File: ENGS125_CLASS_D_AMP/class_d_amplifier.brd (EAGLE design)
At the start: 89.8 x 64.8 mm, 24 parts, among them J1 BANANA_JACK_CT3151, J2 BANANA_JACK_CT3151, J3 BANANA_JACK_CT3151, J4 BANANA_JACK_CT3151, J5 BANANA_JACK_CT3151, J6 BANANA_JACK_CT3151, M1 BSC050NE2LSATMA1, M2 BSC050NE2LSATMA1, U1 LTC6992TSOT-23, U2 LTC4449

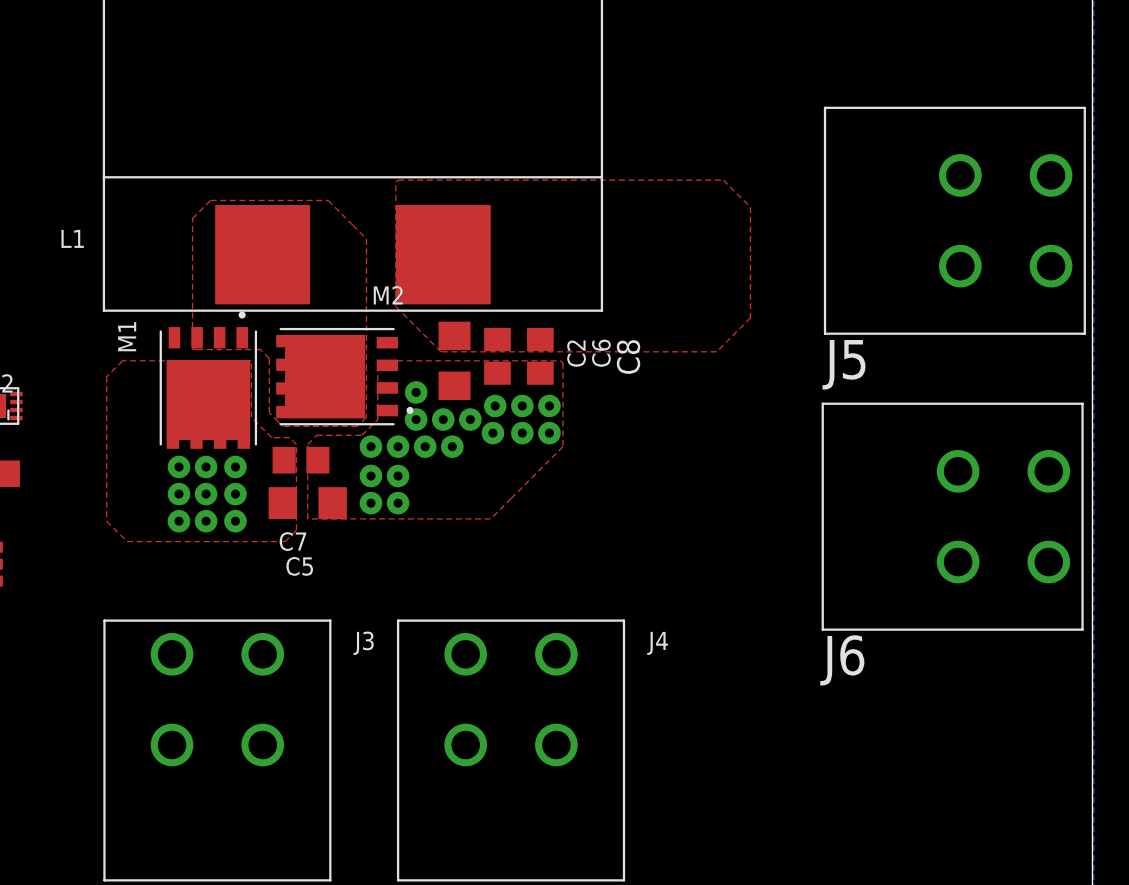
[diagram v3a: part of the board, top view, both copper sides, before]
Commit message: Routed power polygons to connectors
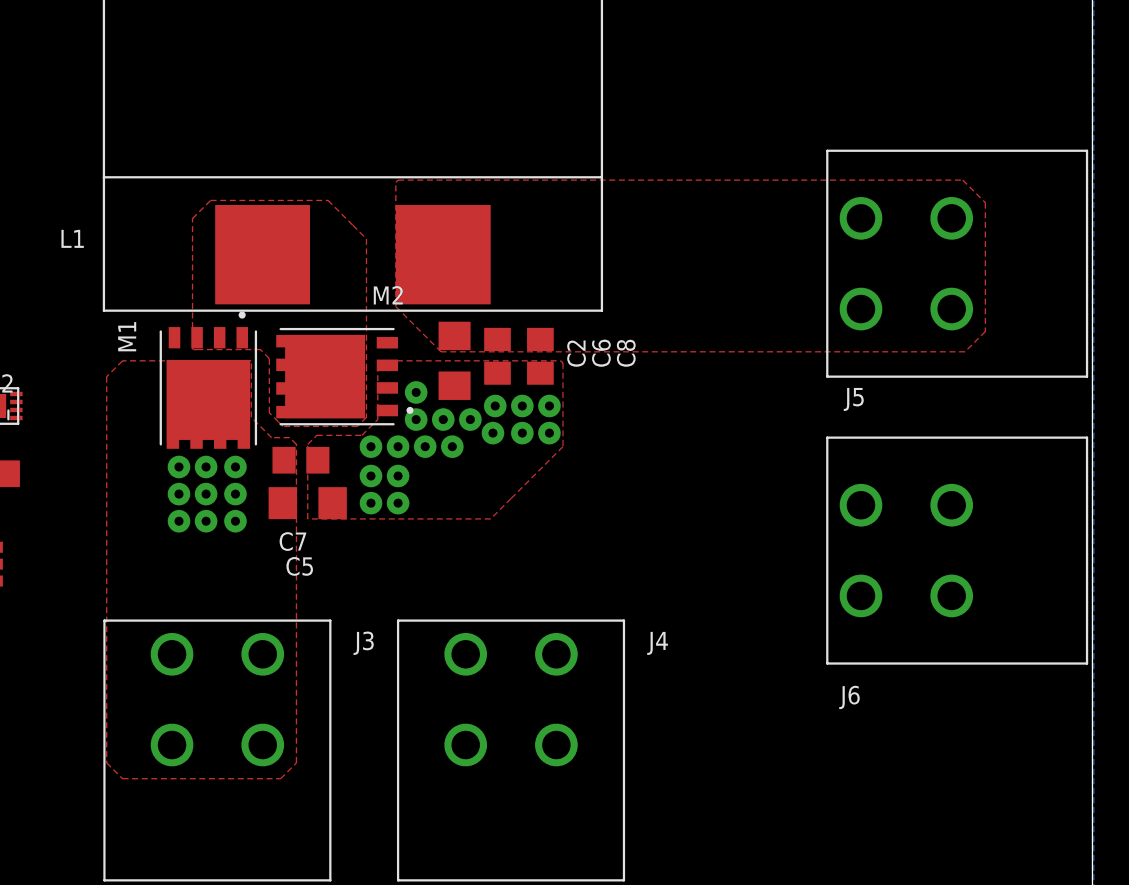
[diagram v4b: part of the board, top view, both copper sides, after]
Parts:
- moved J5 6.09 mm to (79.4, 35.9), turned to 180 degrees
- moved J6 5.78 mm to (79.4, 19.8), turned to 180 degrees
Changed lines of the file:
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@@
 <layer number="17" name="Pads" color="2" fill="1" visible="yes" active="yes"/>
 <layer number="18" name="Vias" color="2" fill="1" visible="yes" active="yes"/>
-<layer number="19" name="Unrouted" color="6" fill="1" visible="no" active="yes"/>
+<layer number="19" name="Unrouted" color="6" fill="1" visible="yes" active="yes"/>
 <layer number="20" name="Dimension" color="24" fill="1" visible="yes" active="yes"/>
 <layer number="21" name="tPlace" color="7" fill="1" visible="yes" active="yes"/>
@@
 <attribute name="NAME" x="51.18835" y="34.66365" size="1.016" layer="25" font="fixed" rot="R180"/>
 </element>
-<element name="J5" library="Engs125_lib_UPDATEFeb22" package="CT3151SP2_PCB_MOUNT" value="BANANA_JACK_CT3151" x="84.963" y="38.354" smashed="yes">
-<attribute name="NAME" x="74.803" y="29.464" size="2.1844" layer="25" font="vector"/>
-</element>
-<element name="J6" library="Engs125_lib_UPDATEFeb22" package="CT3151SP2_PCB_MOUNT" value="BANANA_JACK_CT3151" x="84.836" y="21.717" smashed="yes">
-<attribute name="NAME" x="74.676" y="12.827" size="2.1844" layer="25" font="vector"/>
+<element name="J5" library="Engs125_lib_UPDATEFeb22" package="CT3151SP2_PCB_MOUNT" value="BANANA_JACK_CT3151" x="79.375" y="35.941" smashed="yes" rot="R180">
+<attribute name="NAME" x="77.089" y="28.956" size="1.016" layer="25" font="vector" rot="R180"/>
+</element>
+<element name="J6" library="Engs125_lib_UPDATEFeb22" package="CT3151SP2_PCB_MOUNT" value="BANANA_JACK_CT3151" x="79.375" y="19.812" smashed="yes" rot="R180">
+<attribute name="NAME" x="76.835" y="12.192" size="1.016" layer="25" font="fixed" rot="R180"/>
 </element>
 <element name="C8" library="Engs125_library" package="C0805" value="0.1u" x="58.801" y="30.734" smashed="yes" rot="R270">
-<attribute name="NAME" x="63.119" y="31.75" size="1.27" layer="25" rot="R270"/>
+<attribute name="NAME" x="63.119" y="31.75" size="1.016" layer="25" font="fixed" rot="R270"/>
 </element>
 </elements>
@@
 <vertex x="50.673" y="40.513"/>
 <vertex x="50.8" y="40.64"/>
-<vertex x="69.088" y="40.64"/>
-<vertex x="70.612" y="39.116"/>
-<vertex x="70.612" y="32.893"/>
-<vertex x="68.707" y="30.988"/>
+<vertex x="82.55" y="40.64"/>
+<vertex x="83.82" y="39.37"/>
+<vertex x="83.82" y="32.131"/>
+<vertex x="82.677" y="30.988"/>
 <vertex x="53.213" y="30.988"/>
 </polygon>
-<wire x1="87.513" y1="35.804" x2="87.513" y2="40.904" width="0" layer="19" extent="1-1"/>
-<wire x1="82.413" y1="40.904" x2="87.513" y2="40.904" width="0" layer="19" extent="1-1"/>
-<wire x1="82.413" y1="35.804" x2="87.513" y2="35.804" width="0" layer="19" extent="1-1"/>
-<wire x1="58.801" y1="31.684" x2="82.413" y2="35.804" width="0" layer="19" extent="1-1"/>
 </signal>
 <signal name="VIN">
@@
 <contactref element="M1" pad="6"/>
 <polygon width="0.1524" layer="1" thermals="no">
-<vertex x="35.56" y="20.32"/>
-<vertex x="44.45" y="20.32"/>
-<vertex x="45.085" y="20.955"/>
+<vertex x="35.306" y="6.985"/>
+<vertex x="44.196" y="6.985"/>
+<vertex x="45.085" y="7.874"/>
 <vertex x="45.085" y="25.781"/>
 <vertex x="44.704" y="26.162"/>
@@
 <vertex x="35.306" y="30.48"/>
 <vertex x="34.417" y="29.591"/>
-<vertex x="34.417" y="21.463"/>
+<vertex x="34.417" y="7.874"/>
 </polygon>
 <via x="41.656" y="24.511" extent="1-16" drill="0.508" diameter="1.27"/>
@@
 <via x="40.005" y="21.463" extent="1-16" drill="0.508" diameter="1.27"/>
 <via x="38.481" y="21.463" extent="1-16" drill="0.508" diameter="1.27"/>
-<wire x1="43.19" y1="8.88" x2="43.19" y2="13.98" width="0" layer="19" extent="1-1"/>
-<wire x1="38.09" y1="13.98" x2="43.19" y2="13.98" width="0" layer="19" extent="1-1"/>
-<wire x1="38.09" y1="8.88" x2="43.19" y2="8.88" width="0" layer="19" extent="1-1"/>
-<wire x1="38.481" y1="21.463" x2="38.09" y2="13.98" width="0" layer="19" extent="1-1"/>
 </signal>
 <signal name="BG">

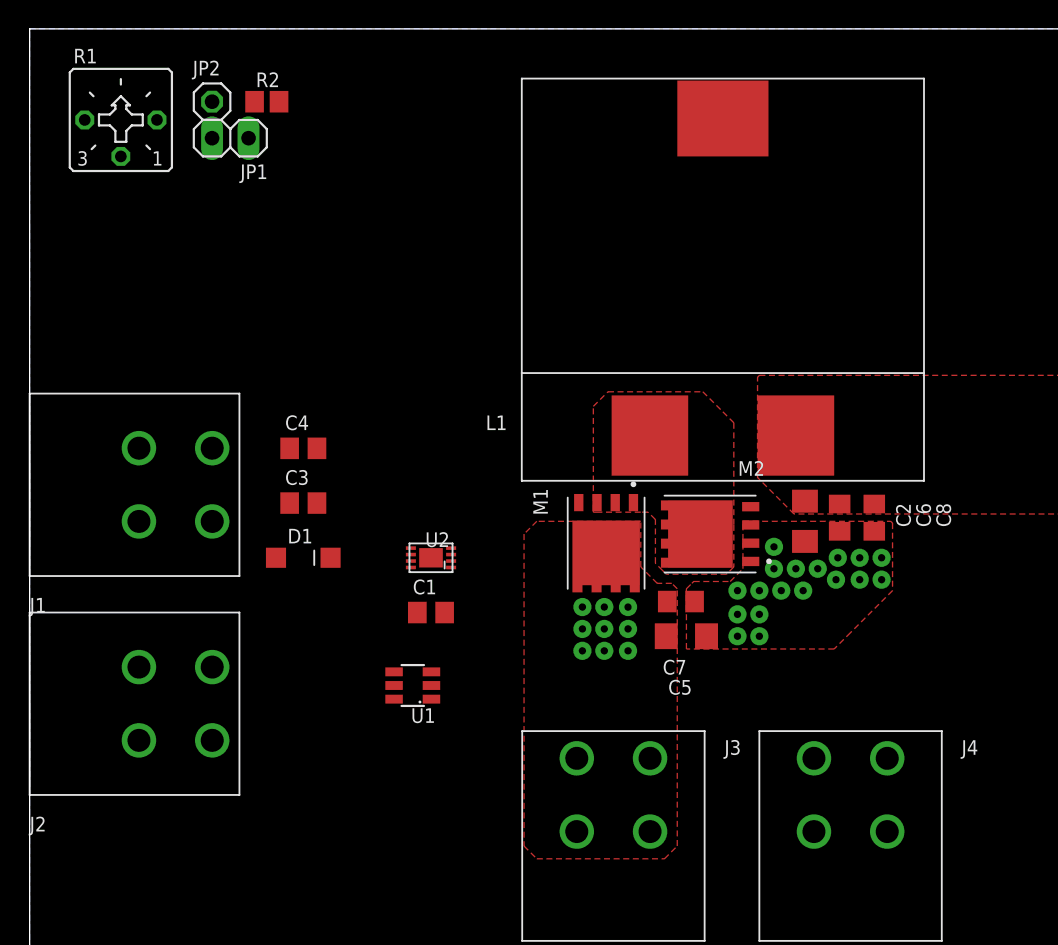
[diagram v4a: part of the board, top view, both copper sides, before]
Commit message: Refined placement of gate driver and PWM modulator ICs
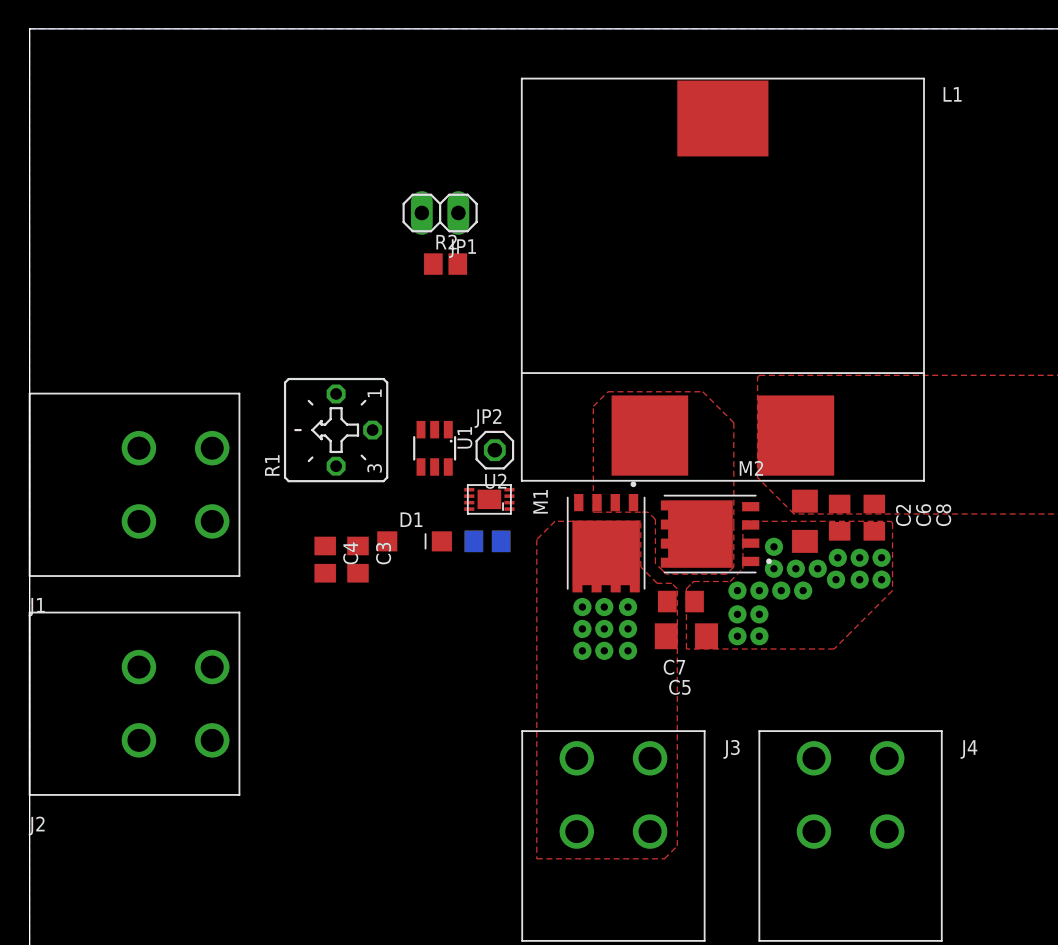
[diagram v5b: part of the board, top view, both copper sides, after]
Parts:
- moved JP2 31.2 mm to (32.4, 35.4)
- moved R1 26.3 mm to (21.3, 36.8), turned to 90 degrees
- moved R2 16.8 mm to (29.0, 48.4)
- moved U1 16.6 mm to (28.2, 35.6), turned to 180 degrees
- moved JP1 15.5 mm to (28.6, 51.9)
- moved C4 7.90 mm to (20.6, 27.8), turned to 270 degrees
- moved D1 7.83 mm to (26.8, 29.1)
- moved C1 6.33 mm to (31.9, 29.1), flipped to the bottom, turned to 180 degrees
- moved U2 5.75 mm to (32.0, 32.0)
- moved C3 5.48 mm to (22.9, 27.8), turned to 270 degrees
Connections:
- net GND: no longer JP1.1, JP1.2
- net N$1: now also R1.S; no longer R1.A
- net N$4: now also JP1.1, JP1.2

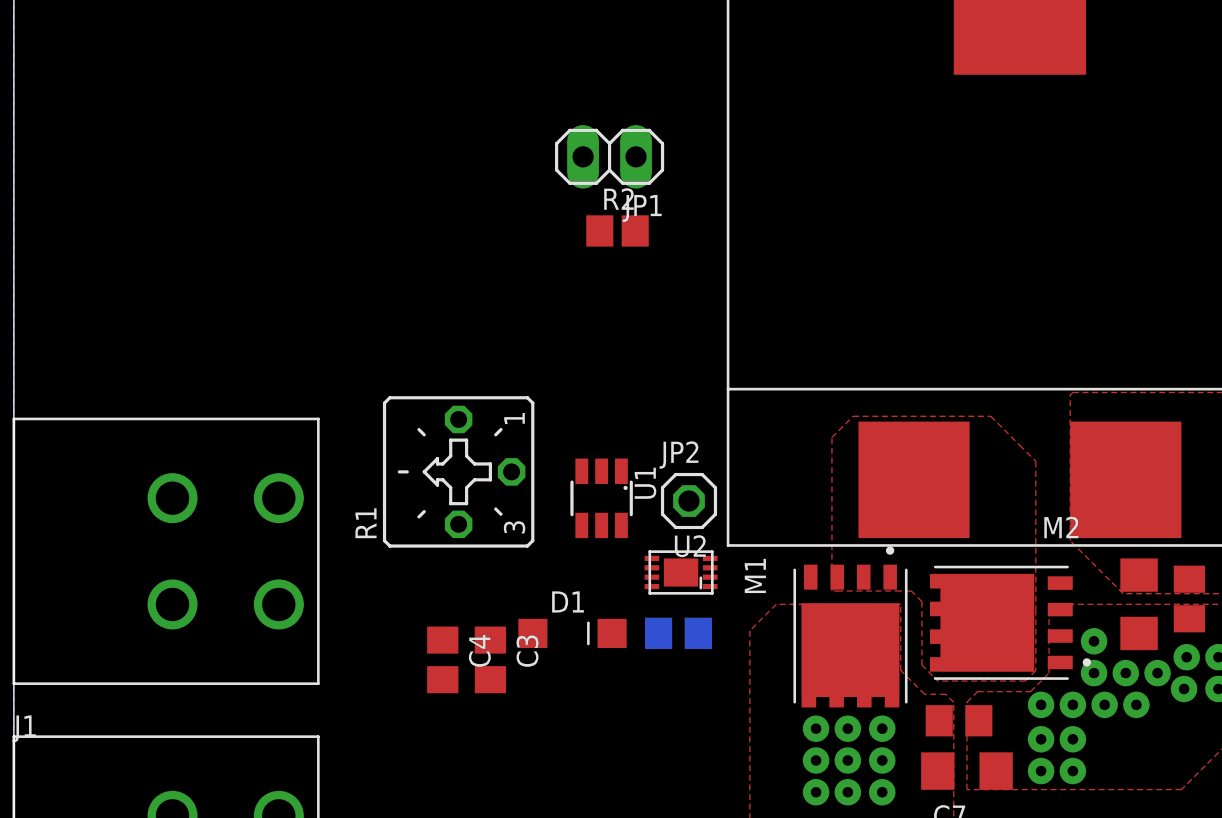
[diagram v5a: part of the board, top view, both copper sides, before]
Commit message: Routed top layer signals
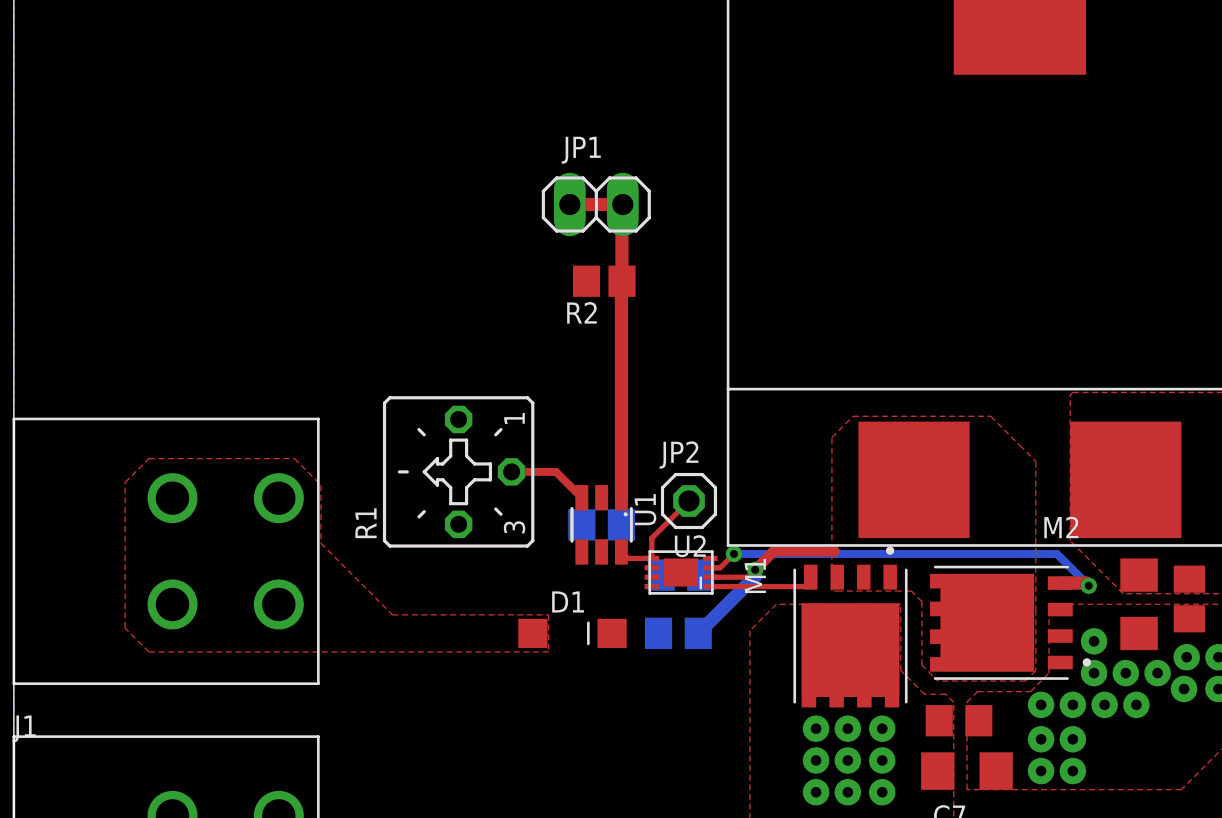
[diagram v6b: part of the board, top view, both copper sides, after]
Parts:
- moved C4 12.1 mm to (32.0, 31.9), flipped to the bottom, turned to 180 degrees
- moved C3 8.39 mm to (28.2, 34.3), flipped to the bottom, turned to 180 degrees
- moved R2 2.50 mm to (28.3, 46.0)
- moved JP1 2.37 mm to (27.9, 49.7)
- moved U1 1.27 mm to (28.2, 34.3)
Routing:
- net BG: track 0.00 -> 20.5 mm, vias 0 -> 2
- net N$4: track 0.00 -> 16.6 mm
- net VSW: track 0.00 -> 10.7 mm, vias 0 -> 1
- net TG: track 0.00 -> 5.27 mm
- net VPWM: track 0.00 -> 5.08 mm
- net N$1: track 0.00 -> 3.88 mm
- added copper zone on layer 1, net VGG
